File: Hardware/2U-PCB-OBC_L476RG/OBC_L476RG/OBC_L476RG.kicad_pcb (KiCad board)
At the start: 2 copper layers, 90 x 92 mm, 7 parts, among them J1 Bus Standard, J2 Micro_SD_Card_Det_Hirose_DM3AT, U2 NUCLEO_L476RG

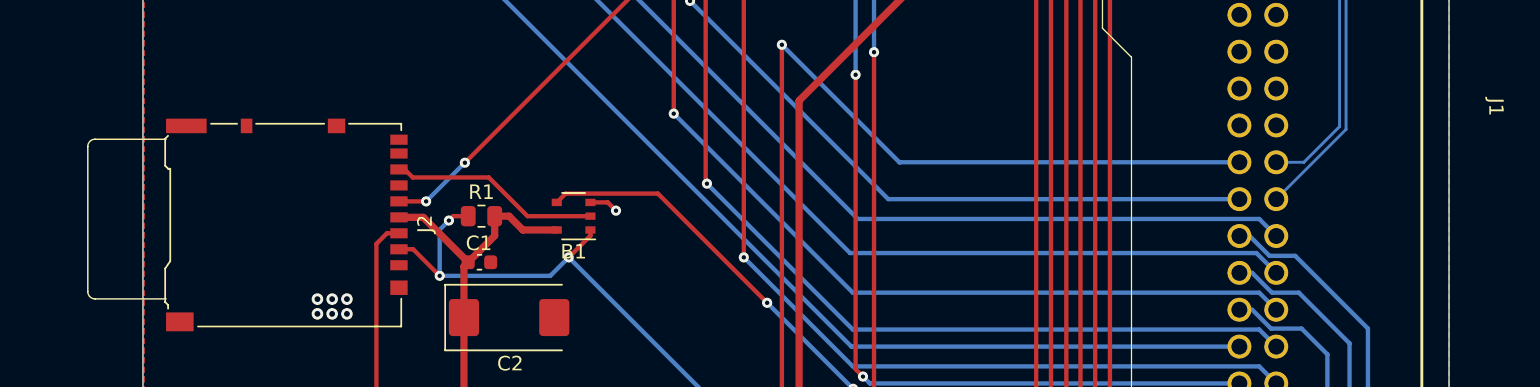
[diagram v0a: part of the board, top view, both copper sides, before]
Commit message: Project name was wrong in in kicad files. Project renamed
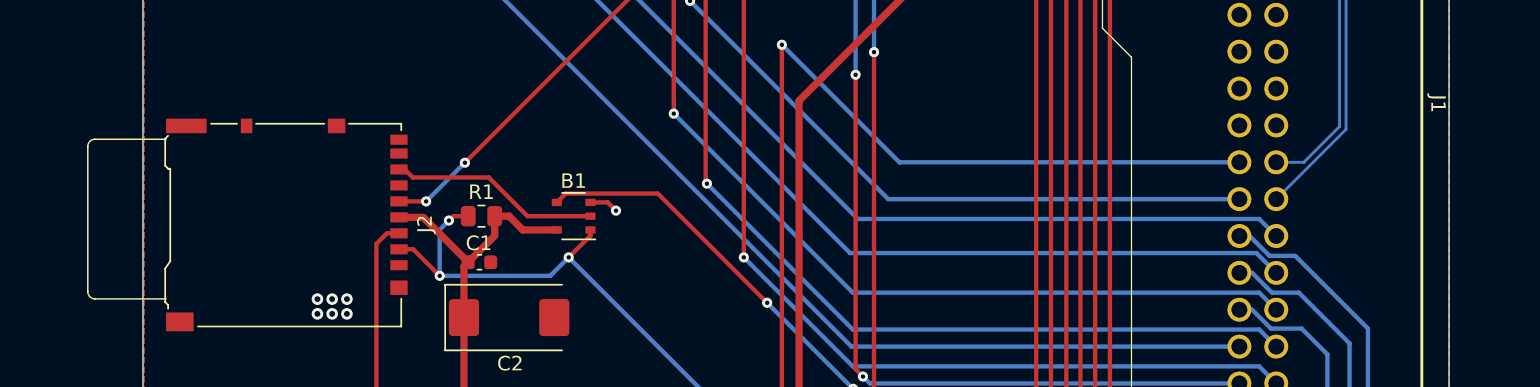
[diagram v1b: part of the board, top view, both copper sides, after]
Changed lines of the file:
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@@
     (property "Sheetname" "")
     (attr through_hole)
-    (fp_text reference "J1" (at 4.8612 -7.621576 -90 unlocked) (layer "F.SilkS")
+    (fp_text reference "J1" (at 0.868 -7.85 -90 unlocked) (layer "F.SilkS")
         (effects (font (size 1 1) (thickness 0.1)))
     )
@@
     (property "Sheetname" "")
     (attr smd)
-    (fp_text reference "B1" (at 0 -2.45) (layer "F.SilkS")
+    (fp_text reference "B1" (at 0 2.413) (layer "F.SilkS")
         (effects (font (size 1 1) (thickness 0.15)))
     )
@@
     (fp_arc (start -5.407341 13.716803) (mid -5.760894 13.570356) (end -5.907341 13.216803)
       (stroke (width 0.1) (type solid)) (layer "F.SilkS"))
-    (fp_arc (start 5.092659 13.216803) (mid 4.946211 13.570354) (end 4.592659 13.716803)
+    (fp_arc (start 5.092659 13.216803) (mid 4.946212 13.570358) (end 4.592659 13.716803)
       (stroke (width 0.1) (type solid)) (layer "F.SilkS"))
     (fp_line (start -7.82 -8.82) (end 7.88 -8.82)
